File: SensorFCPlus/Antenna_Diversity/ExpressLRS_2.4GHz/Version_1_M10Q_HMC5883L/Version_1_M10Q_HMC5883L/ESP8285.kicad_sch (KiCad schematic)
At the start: 24 parts, among them U5 ESP8285H16, Y1 26MHz

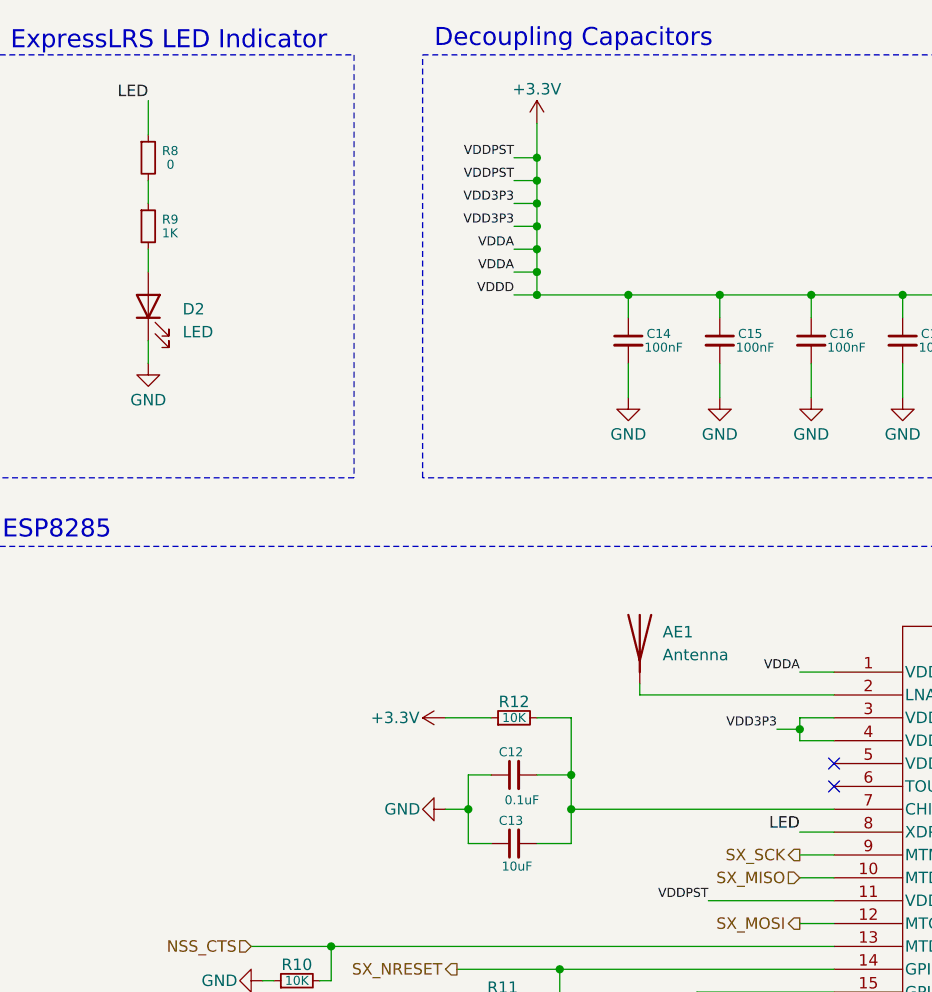
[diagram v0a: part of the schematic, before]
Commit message: Updated README and V1 M10Q HMC5883L KiCad files, added documentation and media
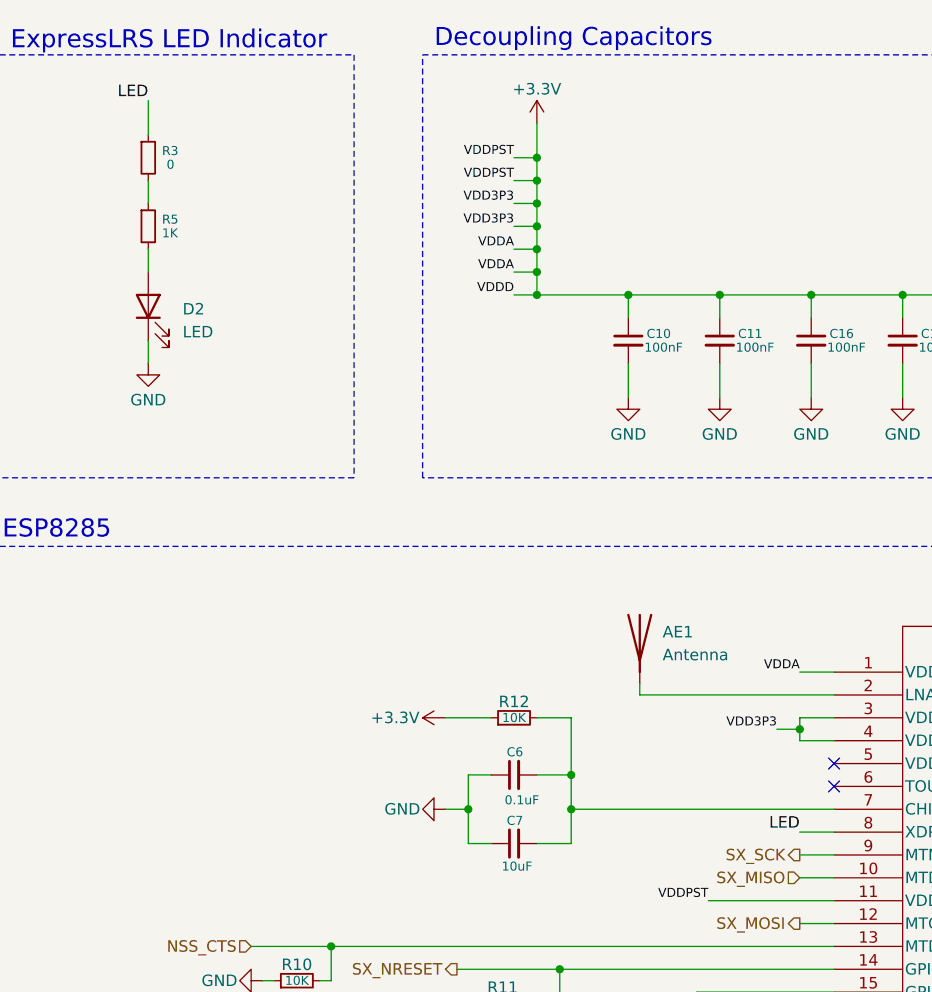
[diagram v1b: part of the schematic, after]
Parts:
- removed C12: 0.1uF, Capacitor_SMD:C_0805_2012Metric_Pad1.18x1.45mm_HandSolder, symbol Device:C_Small
- removed C13: 10uF, ECASD40J106M055K00:ECASD40J106M055K00, symbol Device:C_Small
- removed C14, C15: 100nF, Capacitor_SMD:C_0805_2012Metric_Pad1.18x1.45mm_HandSolder, symbol Device:C_Small
- removed R8: 0, Resistor_SMD:R_0805_2012Metric_Pad1.20x1.40mm_HandSolder, symbol Device:R_Small
- removed R9: 1K, Resistor_SMD:R_0805_2012Metric_Pad1.20x1.40mm_HandSolder, symbol Device:R_Small
- added C10, C11: 100nF, Capacitor_SMD:C_0805_2012Metric_Pad1.18x1.45mm_HandSolder, symbol Device:C_Small
- added C6: 0.1uF, Capacitor_SMD:C_0805_2012Metric_Pad1.18x1.45mm_HandSolder, symbol Device:C_Small
- added C7: 10uF, ECASD40J106M055K00:ECASD40J106M055K00, symbol Device:C_Small
- added R3: 0, Resistor_SMD:R_0805_2012Metric_Pad1.20x1.40mm_HandSolder, symbol Device:R_Small
- added R5: 1K, Resistor_SMD:R_0805_2012Metric_Pad1.20x1.40mm_HandSolder, symbol Device:R_Small
- JP1: footprint TestPoint:TestPoint_2Pads_Pitch2.54mm_Drill0.8mm -> Jumper:SolderJumper-2_P1.3mm_Open_RoundedPad1.0x1.5mm
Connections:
- net +3.3V: now also C10.1, C11.1
- net GND: now also C10.2, C11.2, C6.1, C7.1
- net LED: now also R3.1
- net at R12.2, U5.7 (CHIP_EN): now also C6.2, C7.2
- net at D2.2 (A): now also R5.2
- new net: R3.2, R5.1
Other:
- title: (none) -> ESP8285
